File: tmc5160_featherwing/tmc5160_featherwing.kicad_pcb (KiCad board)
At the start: 2 copper layers, 50.8 x 22.9 mm, 11 parts, among them U1 TMC5160A-WA, U2 BUK7D36-60EX, U3 BUK7D36-60EX

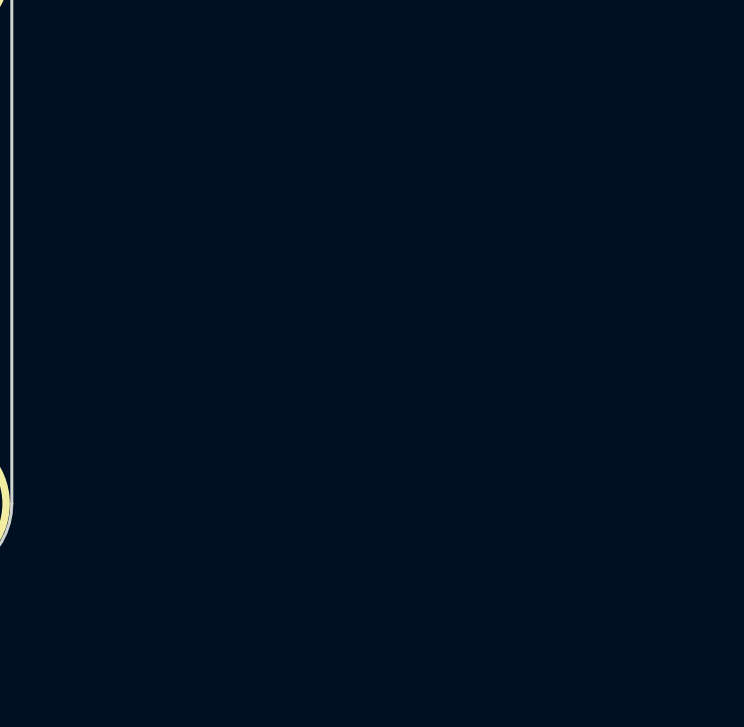
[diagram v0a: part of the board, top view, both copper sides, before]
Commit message: Add gate resistors
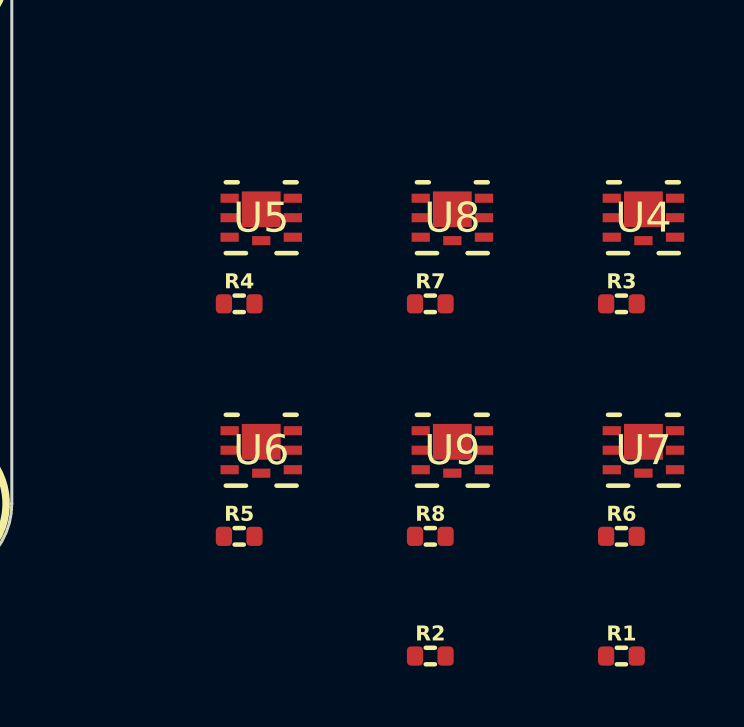
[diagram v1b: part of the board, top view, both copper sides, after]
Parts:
- added R1: 15, Janelia:R_0402_1005Metric, F.Cu at (198.1, 115.6)
- added R2: 15, Janelia:R_0402_1005Metric, F.Cu at (191.8, 115.6)
- added R3: 15, Janelia:R_0402_1005Metric, F.Cu at (198.1, 103.8)
- added R4: 15, Janelia:R_0402_1005Metric, F.Cu at (185.4, 103.8)
- added R5: 15, Janelia:R_0402_1005Metric, F.Cu at (185.4, 111.6)
- added R6: 15, Janelia:R_0402_1005Metric, F.Cu at (198.1, 111.6)
- added R7: 15, Janelia:R_0402_1005Metric, F.Cu at (191.8, 103.8)
- added R8: 15, Janelia:R_0402_1005Metric, F.Cu at (191.8, 111.6)
- added U4: BUK7D36-60EX, Janelia:BUK7D3660EX_NEX, F.Cu at (198.9, 101.0)
- added U5: BUK7D36-60EX, Janelia:BUK7D3660EX_NEX, F.Cu at (186.1, 101.0)
- added U6: BUK7D36-60EX, Janelia:BUK7D3660EX_NEX, F.Cu at (186.1, 108.7)
- added U7: BUK7D36-60EX, Janelia:BUK7D3660EX_NEX, F.Cu at (198.9, 108.7)
- added U8: BUK7D36-60EX, Janelia:BUK7D3660EX_NEX, F.Cu at (192.5, 101.0)
- added U9: BUK7D36-60EX, Janelia:BUK7D3660EX_NEX, F.Cu at (192.5, 108.7)
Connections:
- U2 pad 1: unconnected-(U2-D-Pad1) -> /driver_controller/mosfet1/DRAIN
- U2 pad 2: unconnected-(U2-D-Pad2) -> /driver_controller/mosfet1/DRAIN
- U2 pad 3: unconnected-(U2-G-Pad3) -> Net-(U2-G)
- U2 pad 4: unconnected-(U2-S-Pad4) -> /driver_controller/mosfet1/SOURCE
- U2 pad 5: unconnected-(U2-D-Pad5) -> /driver_controller/mosfet1/DRAIN
- U2 pad 6: unconnected-(U2-D-Pad6) -> /driver_controller/mosfet1/DRAIN
- U2 pad 7: unconnected-(U2-D-Pad7) -> /driver_controller/mosfet1/DRAIN
- U2 pad 8: unconnected-(U2-S-Pad8) -> /driver_controller/mosfet1/SOURCE
- U3 pad 1: unconnected-(U3-D-Pad1) -> /driver_controller/mosfet2/DRAIN
- U3 pad 2: unconnected-(U3-D-Pad2) -> /driver_controller/mosfet2/DRAIN
- U3 pad 3: unconnected-(U3-G-Pad3) -> Net-(U3-G)
- U3 pad 4: unconnected-(U3-S-Pad4) -> /driver_controller/mosfet2/SOURCE
- U3 pad 5: unconnected-(U3-D-Pad5) -> /driver_controller/mosfet2/DRAIN
- U3 pad 6: unconnected-(U3-D-Pad6) -> /driver_controller/mosfet2/DRAIN
- U3 pad 7: unconnected-(U3-D-Pad7) -> /driver_controller/mosfet2/DRAIN
- U3 pad 8: unconnected-(U3-S-Pad8) -> /driver_controller/mosfet2/SOURCE

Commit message: Add connectors
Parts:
- added J1: Conn_TERM_HDR_01x02_Pin_5.0MM_Horizontal, Janelia:PhoenixContact_MSTBA_2,5_2-G_1x02_P5.00mm_Horizontal, F.Cu at (126.2, 99.1)
- added J2: Conn_TERM_HDR_01x04_Pin_3.5MM_Horizontal, Janelia:PhoenixContact_MC_1,5_4-G-3.5_1x04_P3.50mm_Horizontal, F.Cu at (180.5, 106.8)
- added J3: Conn_01x16_P2.54MM_HeaderHoles, Janelia:PinHeader_1x16_P2.54mm_Vertical_Holes, F.Cu at (133.3, 111.8)
- added J4: Conn_01x12_P2.54MM_HeaderHoles, Janelia:PinHeader_1x12_P2.54mm_Vertical_Holes, F.Cu at (143.5, 91.4)
- moved U2 46.7 mm to (198.1, 66.0)
- moved U3 45.0 mm to (198.1, 72.4)
- moved R1 38.6 mm to (186.7, 78.7)
- moved R2 38.6 mm to (180.3, 78.7)
- moved R3 38.6 mm to (186.7, 67.0)
- moved R4 38.6 mm to (173.9, 67.0)
- moved R5 38.6 mm to (173.9, 74.8)
- moved R6 38.6 mm to (186.7, 74.8)
- moved R7 38.6 mm to (180.3, 67.0)
- moved R8 38.6 mm to (180.3, 74.8)
- moved U5 38.6 mm to (174.7, 64.1)
- moved U6 38.6 mm to (174.7, 71.9)
- moved U8 38.6 mm to (181.1, 64.1)
- moved U9 38.6 mm to (181.1, 71.9)
- moved U4 38.6 mm to (187.4, 64.1)
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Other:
- board size 50.8 x 22.9 mm -> 72 x 22.9 mm

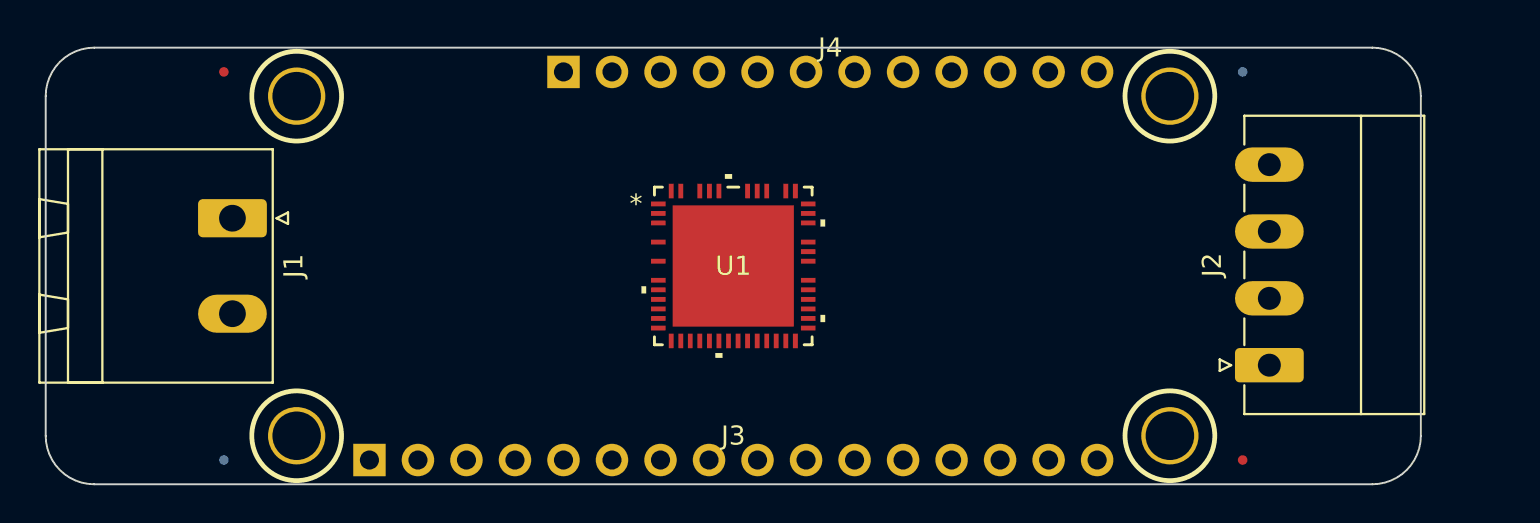
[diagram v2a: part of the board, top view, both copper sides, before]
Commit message: Change connectors
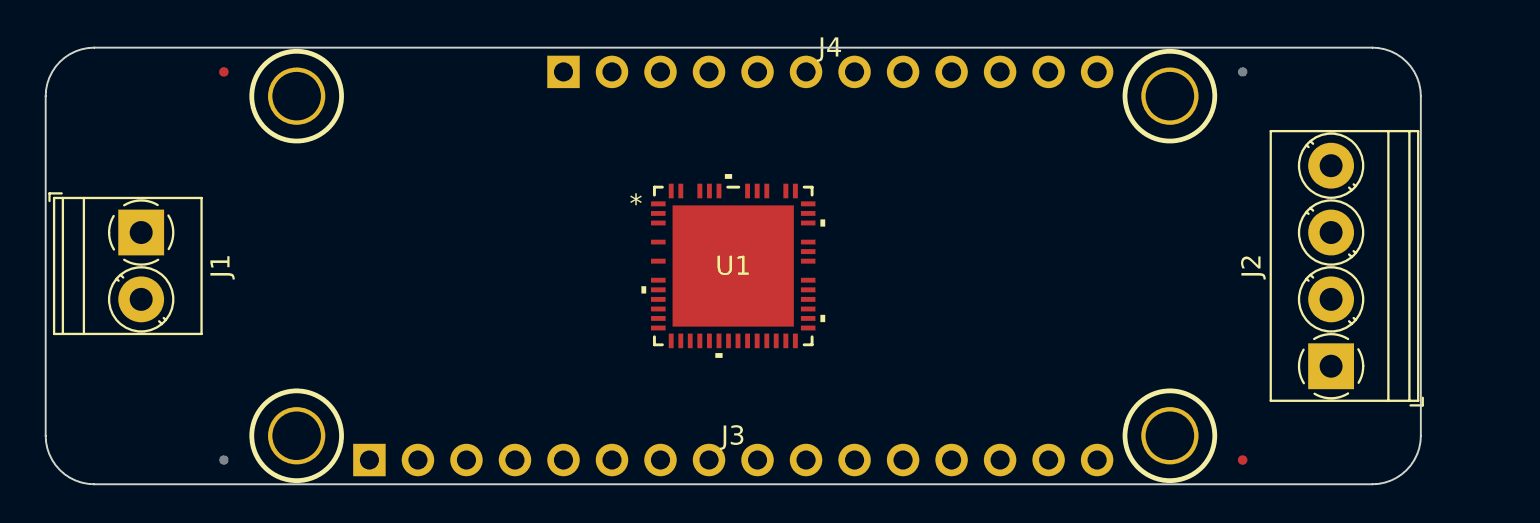
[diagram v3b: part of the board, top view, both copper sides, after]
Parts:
- J1: value Conn_TERM_HDR_01x02_Pin_5.0MM_Horizontal -> Screw_Terminal_01x02_P3.5MM_Horizontal; footprint Janelia:PhoenixContact_MSTBA_2,5_2-G_1x02_P5.00mm_Horizontal -> Janelia:TerminalBlock_Phoenix_PT-1,5-2-3.5-H_1x02_P3.50mm_Horizontal
- J2: value Conn_TERM_HDR_01x04_Pin_3.5MM_Horizontal -> Screw_Terminal_01x04_P3.5MM_Horizontal; footprint Janelia:PhoenixContact_MC_1,5_4-G-3.5_1x04_P3.50mm_Horizontal -> Janelia:TerminalBlock_Phoenix_PT-1,5-4-3.5-H_1x04_P3.50mm_Horizontal
- moved J1 4.84 mm to (121.4, 99.8)
- moved J2 3.23 mm to (183.7, 106.8)

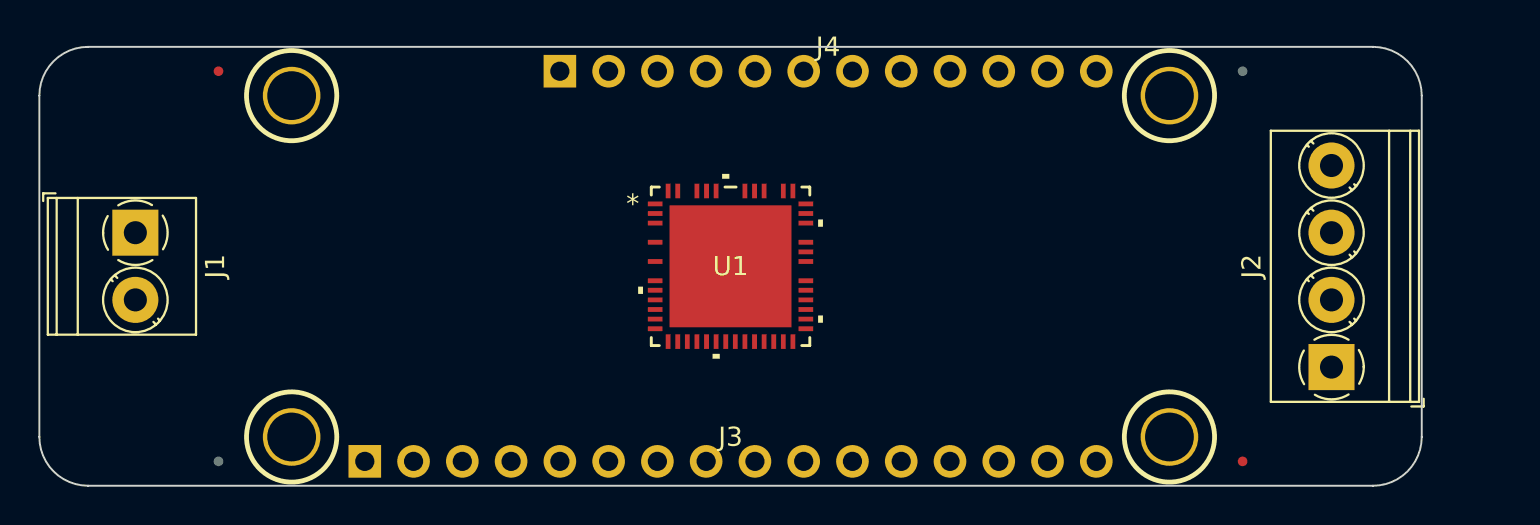
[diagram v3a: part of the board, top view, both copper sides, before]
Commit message: Switch back to terminal blocks
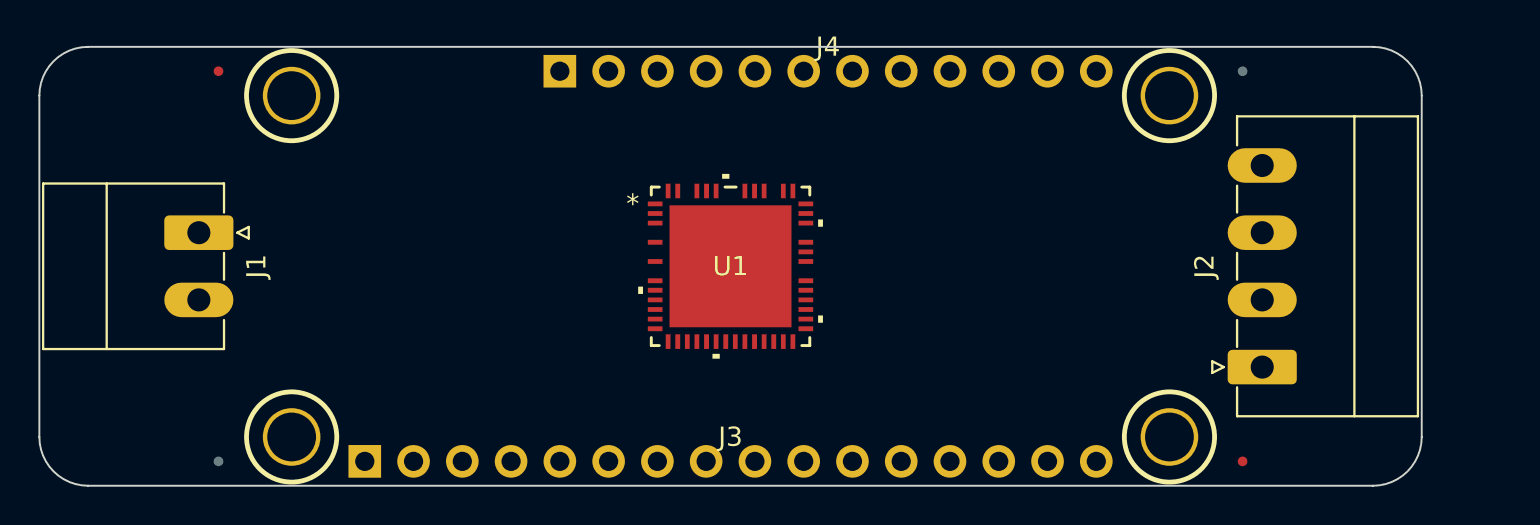
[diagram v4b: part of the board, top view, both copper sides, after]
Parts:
- J1: value Screw_Terminal_01x02_P3.5MM_Horizontal -> Conn_TERM_HDR_01x02_Pin_3.5MM_Horizontal; footprint Janelia:TerminalBlock_Phoenix_PT-1,5-2-3.5-H_1x02_P3.50mm_Horizontal -> Janelia:PhoenixContact_MC_1,5_2-G-3.5_1x02_P3.50mm_Horizontal
- J2: value Screw_Terminal_01x04_P3.5MM_Horizontal -> Conn_TERM_HDR_01x04_Pin_3.5MM_Horizontal; footprint Janelia:TerminalBlock_Phoenix_PT-1,5-4-3.5-H_1x04_P3.50mm_Horizontal -> Janelia:PhoenixContact_MC_1,5_4-G-3.5_1x04_P3.50mm_Horizontal
- moved J2 6.37 mm to (180.1, 101.6)
- moved J1 3.74 mm to (124.7, 101.6)

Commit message: Add push option
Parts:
- J2: value Conn_TERM_HDR_01x04_Pin_3.5MM_Horizontal -> Conn_01x04_P3.5MM_TBH_Horizontal_Screw; footprint Janelia:PhoenixContact_MC_1,5_4-G-3.5_1x04_P3.50mm_Horizontal -> Janelia:PhoenixContact_MC_1,5_4-G-3.5_1x04_P3.50mm_Horizontal_Push
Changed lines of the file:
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@@
     )
   )
-  (footprint "Janelia:PhoenixContact_MC_1,5_4-G-3.5_1x04_P3.50mm_Horizontal" (layer "F.Cu")
+  (footprint "Janelia:PhoenixContact_MC_1,5_4-G-3.5_1x04_P3.50mm_Horizontal_Push" (layer "F.Cu")
     (at 180.0925 101.6 90)
     (descr "Generic Phoenix Contact connector footprint for: MC_1,5/4-G-3.5; number of pins: 04; pin pitch: 3.50mm; Angled || order number: 1844236 8A 160V")
@@
         (effects (font (size 1 1) (thickness 0.15)))
     )
-    (fp_text value "Conn_TERM_HDR_01x04_Pin_3.5MM_Horizontal" (at 0 9.2 90) (layer "F.Fab")
+    (fp_text value "Conn_01x04_P3.5MM_TBH_Horizontal_Screw" (at 0 9.2 90) (layer "F.Fab")
         (effects (font (size 1 1) (thickness 0.15)))
     )
@@
       (rotate (xyz 0 0 0))
     )
-    (model "${KICAD_JANELIA_LIBRARY}/3dmodels/Janelia.3dshapes/1840382.step"
-      (offset (xyz -7.05 -16.25 -3.7))
+    (model "${KICAD_JANELIA_LIBRARY}/3dmodels/Janelia.3dshapes/1952283.step"
+      (offset (xyz -7.05 -22.75 0.3))
       (scale (xyz 1 1 1))
       (rotate (xyz 0 0 0))

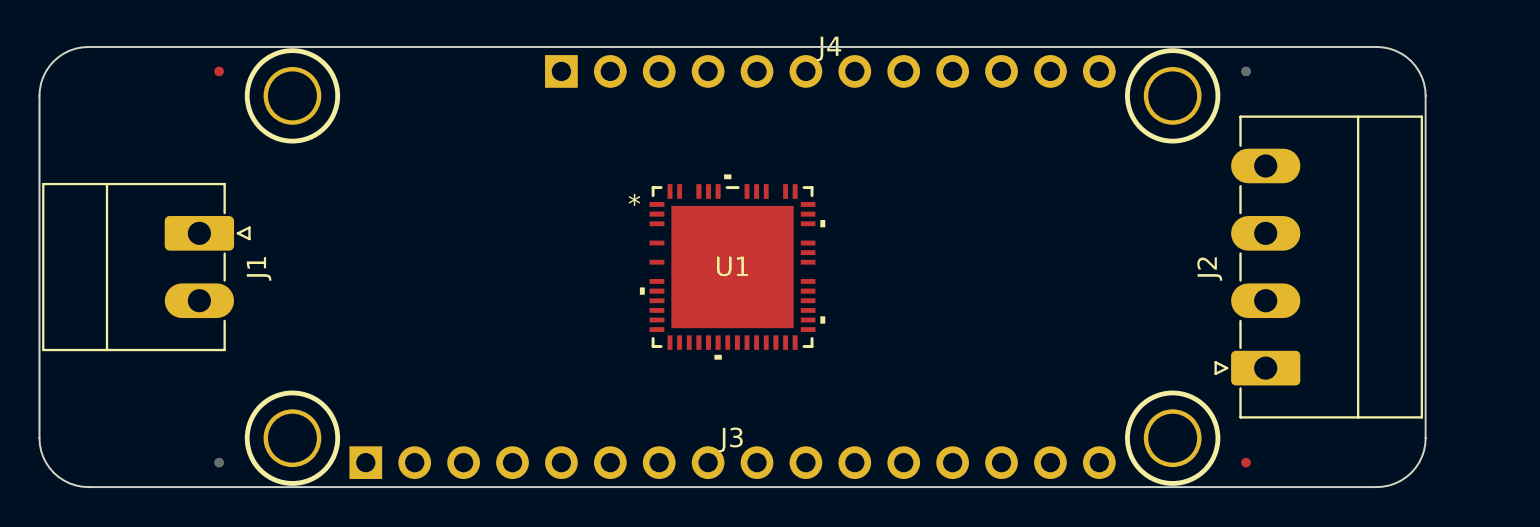
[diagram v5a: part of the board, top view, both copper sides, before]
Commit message: Adjust connectors
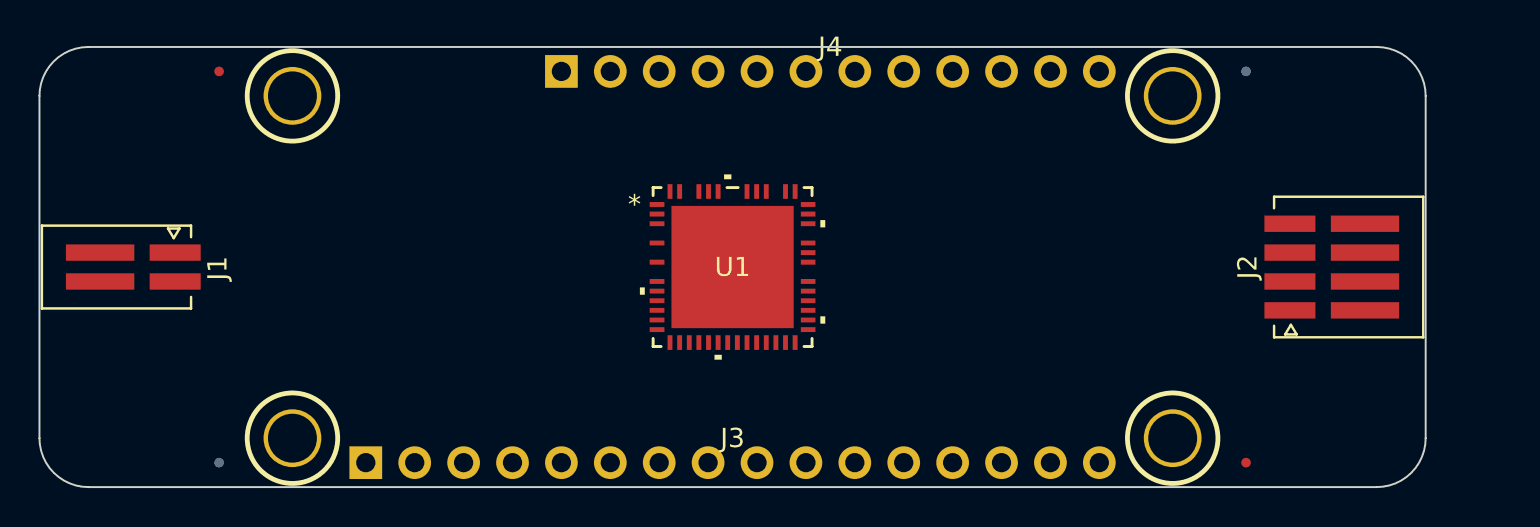
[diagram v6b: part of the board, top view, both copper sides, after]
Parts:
- J1: value Conn_TERM_HDR_01x02_Pin_3.5MM_Horizontal -> Conn_01x02_P1.5MM_Molex_Pico-SPOX_Horizontal; footprint Janelia:PhoenixContact_MC_1,5_2-G-3.5_1x02_P3.50mm_Horizontal -> Janelia:Molex_Pico-SPOX_87438_1x02-P1.5MM_Horizontal
- J2: value Conn_01x04_P3.5MM_TBH_Horizontal_Screw -> Conn_01x04_P1.5MM_Molex_Pico-SPOX_Horizontal; footprint Janelia:PhoenixContact_MC_1,5_4-G-3.5_1x04_P3.50mm_Horizontal_Push -> Janelia:Molex_Pico-SPOX_87438_1x04-P1.5mm_Horizontal
- moved J2 4.31 mm to (184.4, 101.6)
- moved J1 4.31 mm to (120.4, 101.6)

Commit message: Add to power sheet
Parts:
- added C1: 100uF_63V, Janelia:CP_Elec_10x10.5, F.Cu at (123.2, 101.6)
- added C2: 10uF_100V, Janelia:C_1210_3225Metric, F.Cu at (133.3, 101.6)
- added C3: 10uF_6.3V, Janelia:C_0402_1005Metric, F.Cu at (138.4, 106.7)
- added J5: Conn_01x02_P1.5MM_Molex_Pico-SPOX_Horizontal, Janelia:Molex_Pico-Clasp-501568_1x02_P1MM_Horizontal, B.Cu at (184.9, 108.1)
- added J6: Conn_01x16_P2.54MM_HeaderHoles, Janelia:PinHeader_1x16_P2.54mm_Vertical_Holes, F.Cu at (133.3, 111.8)
- added J7: Conn_01x12_P2.54MM_HeaderHoles, Janelia:PinHeader_1x12_P2.54mm_Vertical_Holes, F.Cu at (143.5, 91.4)
- added U10: 3.3V_100MA, Janelia:DRB0008B, F.Cu at (130.8, 101.6)
- J1: value Conn_01x02_P1.5MM_Molex_Pico-SPOX_Horizontal -> Conn_01x03_P2.54MM_HeaderHoles; footprint Janelia:Molex_Pico-SPOX_87438_1x02-P1.5MM_Horizontal -> Janelia:PinHeader_1x03_P2.54mm_Vertical_Holes
- J2: value Conn_01x04_P1.5MM_Molex_Pico-SPOX_Horizontal -> Conn_01x02_P1.5MM_Molex_Pico-SPOX-87438_Horizontal; footprint Janelia:Molex_Pico-SPOX_87438_1x04-P1.5mm_Horizontal -> Janelia:Molex_Pico-SPOX-87438_1x02-P1.5MM_Horizontal; moved to B.Cu
- J3: value Conn_01x16_P2.54MM_HeaderHoles -> Conn_01x03_P2.54MM_HeaderHoles; footprint Janelia:PinHeader_1x16_P2.54mm_Vertical_Holes -> Janelia:PinHeader_1x03_P2.54mm_Vertical_Holes
- J4: value Conn_01x12_P2.54MM_HeaderHoles -> Conn_01x04_P1.5MM_Molex_Pico-SPOX-87438_Horizontal; footprint Janelia:PinHeader_1x12_P2.54mm_Vertical_Holes -> Janelia:Molex_Pico-SPOX-87438_1x04-P1.5mm_Horizontal; moved to B.Cu
- moved J2 63.8 mm to (120.7, 101.6)
- moved J4 41.9 mm to (184.2, 101.6), turned to -90 degrees
- moved J3 12.7 mm to (120.7, 111.8)
- moved J1 10.2 mm to (120.7, 91.4), turned to 90 degrees
- moved FID2 8.33 mm to (187.4, 91.6)
- moved FID3 8.33 mm to (187.4, 111.6)
- moved FID1 8.33 mm to (117.4, 91.6)
- moved FID4 8.33 mm to (117.4, 111.6)
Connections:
- J1 pad 1: unconnected-(J1-Pin_1-Pad1) -> /VM
- J1 pad 2: unconnected-(J1-Pin_2-Pad2) -> /VM
- J2 pad 1: unconnected-(J2-Pin_1-Pad1) -> /VM
- J2 pad 2: unconnected-(J2-Pin_2-Pad2) -> /GND
- J3 pad 1: unconnected-(J3-Pin_1-Pad1) -> /GND
- J3 pad 2: unconnected-(J3-Pin_2-Pad2) -> /GND
- J3 pad 3: unconnected-(J3-Pin_3-Pad3) -> /GND

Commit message: Add parts
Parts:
- added C4: 10uF_6.3V, Janelia:C_0402_1005Metric, F.Cu at (154.9, 74.9)
- added D1: Diode_SMAJ51A, Janelia:D_SMA, F.Cu at (151.1, 101.6)
- added U11: MAX6816, Janelia:SOT192P237X122-4N, F.Cu at (172.7, 102.9)
- added X1: 16MHz, Janelia:OSC_ECS-2520S33-160-FN-TR, F.Cu at (154.9, 108.0)
- C2: value 10uF_100V -> 100uF_63V; footprint Janelia:C_1210_3225Metric -> Janelia:CP_Elec_10x10.5
- C3: value 10uF_6.3V -> 10uF_100V; footprint Janelia:C_0402_1005Metric -> Janelia:C_1210_3225Metric
- J2, J4, J5: moved to F.Cu
- moved C3 46.6 mm to (161.3, 66.0)
- moved U10 43.8 mm to (152.4, 63.5)
- moved C2 10.2 mm to (143.5, 101.6)
- moved C1 8.89 mm to (132.1, 101.6)
- moved U1 8.89 mm to (161.3, 101.6)
- turned J2 to -90 degrees
- turned J4 to 90 degrees
- turned J5 to 90 degrees
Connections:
- C3 pad 1: /VIO -> /VM
- J1 pad 1: /VM -> /GND
- J1 pad 2: /VM -> /GND
- J1 pad 3: /VM -> /GND
- J2 pad 1: /VM -> /GND
- J2 pad 2: /GND -> /VM
- J3 pad 1: /GND -> /VM
- J3 pad 2: /GND -> /VM
- J3 pad 3: /GND -> /VM
- U1 pad 12: unconnected-(U1-TST_MODE-Pad12) -> /GND
- U1 pad 13: unconnected-(U1-CLK-Pad13) -> /driver_controller/CLOCK
- U1 pad 14: unconnected-(U1-~{CS}/CFG3-Pad14) -> /driver_controller/~{CS}
- U1 pad 15: unconnected-(U1-SCK/CFG2-Pad15) -> /driver_controller/SCK
- U1 pad 16: unconnected-(U1-SDI/CFG1-Pad16) -> /driver_controller/MOSI
- U1 pad 17: unconnected-(U1-SDO/CFG0-Pad17) -> /driver_controller/MISO
- U1 pad 19: unconnected-(U1-REFR/DIR-Pad19) -> /GND
- U1 pad 21: unconnected-(U1-SD_MODE-Pad21) -> /GND
- U1 pad 22: unconnected-(U1-SPI_MODE-Pad22) -> /VIO
- U1 pad 25: unconnected-(U1-GNDD-Pad25) -> /GND
- U1 pad 26: unconnected-(U1-ENCN/DCO/CFG6-Pad26) -> /GND
- U1 pad 29: unconnected-(U1-~{DRV_EN}-Pad29) -> /GND
- U1 pad 48: unconnected-(U1-EP-Pad48) -> /GND
- U1 pad 7: unconnected-(U1-GNDA-Pad7) -> /GND
